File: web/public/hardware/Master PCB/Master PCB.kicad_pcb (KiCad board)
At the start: 2 copper layers, 100 x 100 mm, 98 parts, among them J1 Rows 0-15, J10 LDR2, J11 LDR3, J12 LDR4, J13 SWD Conn, J14 LED Conn, J15 OLED1, J16 OLED2, J17 Relay Conn, J2 Cols 0-21, J3 Cols 22-31, J4 5V_IN, J5 LED1, J6 LED2, J7 LED3, J8 LED4, J9 LDR1, Q1 2N7000, Q2 2N7000, Q3 2N7000, Q4 2N7000, SW1 nRST, SW2 Menu Encoder, U1 STM32U585VITx, U2 M95P32-IXMNT, U3 TLV62568DBV, U4 LM339, U5 MAX7375AXR805, U6 USBLC6-4SC6, U7 USBLC6-2SC6, U8 USBLC6-2SC6

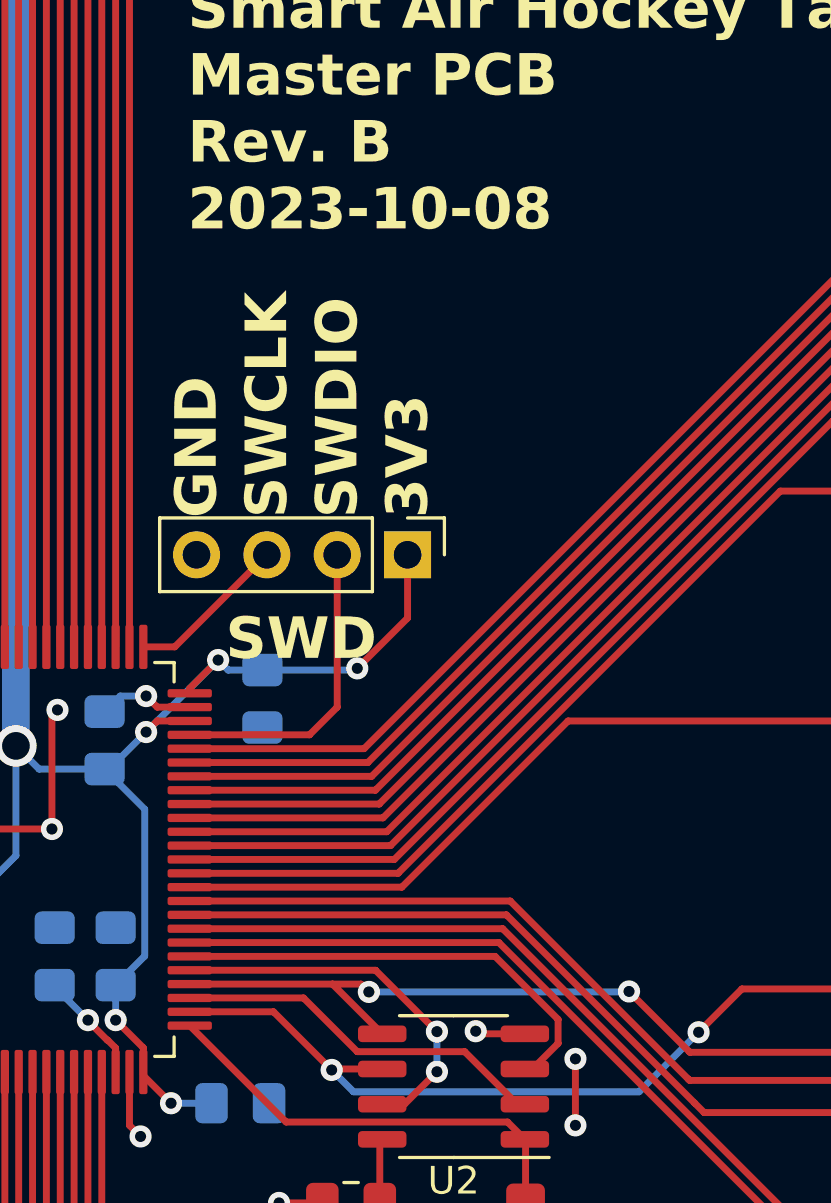
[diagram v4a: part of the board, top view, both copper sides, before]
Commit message: Fix bad trace routing on EEPROM
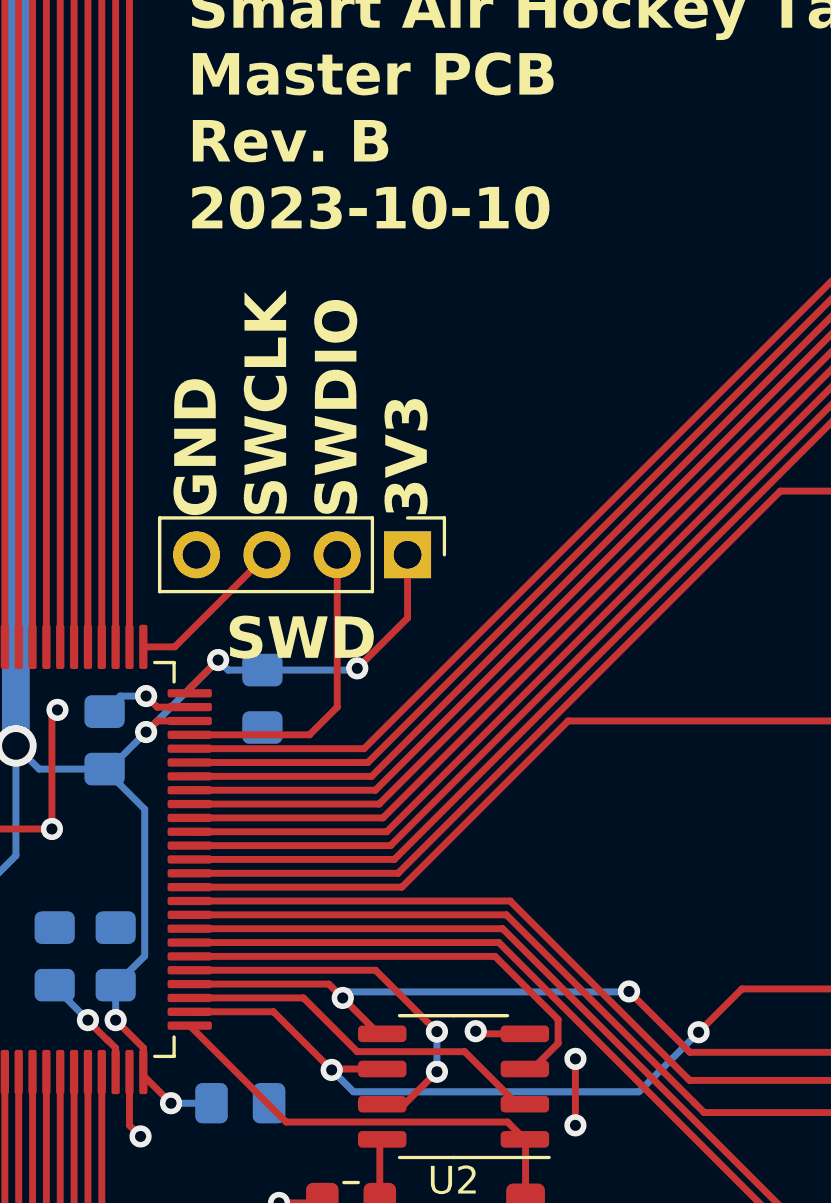
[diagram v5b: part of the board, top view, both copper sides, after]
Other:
- board text added: "ECE 477 Group 5 Smart Air Hockey Table Master PCB Rev. B 2023-10-10"
- board text removed: "ECE 477 Group 5 Smart Air Hockey Table Master PCB Rev. B 2023-10-08"
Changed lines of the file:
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@@
     (effects (font (size 1.5 1.5) (thickness 0.3) bold) (justify top))
   )
-  (gr_text "ECE 477 Group 5\nSmart Air Hockey Table\nMaster PCB\nRev. B\n2023-10-08" (at 157.6 77.4) (layer "F.SilkS")
+  (gr_text "ECE 477 Group 5\nSmart Air Hockey Table\nMaster PCB\nRev. B\n2023-10-10" (at 157.6 77.4) (layer "F.SilkS")
     (effects (font (size 1.5 1.5) (thickness 0.3) bold) (justify left bottom))
   )
@@
   (segment (start 162.8 107.6) (end 163.5895 108.3895) (width 0.25) (layer "B.Cu") (net 42))
   (segment (start 163.5895 108.3895) (end 173.89589 108.3895) (width 0.25) (layer "B.Cu") (net 42))
-  (segment (start 164.625 106.295) (end 162.83 104.5) (width 0.25) (layer "F.Cu") (net 43))
   (segment (start 184.15 106.8625) (end 184.15 105.549503) (width 0.25) (layer "F.Cu") (net 43))
+  (segment (start 164.625 106.295) (end 164.495 106.295) (width 0.25) (layer "F.Cu") (net 43))
   (segment (start 184.15 105.549503) (end 184.100497 105.5) (width 0.25) (layer "F.Cu") (net 43))
+  (segment (start 157.675 104.5) (end 162.7 104.5) (width 0.25) (layer "F.Cu") (net 43))
   (segment (start 198.6755 120.287701) (end 198.6755 112.6755) (width 0.25) (layer "F.Cu") (net 43))
   (segment (start 188.6 108) (end 189.6 109) (width 0.25) (layer "F.Cu") (net 43))
+  (segment (start 164.495 106.295) (end 163.2 105) (width 0.25) (layer "F.Cu") (net 43))
   (segment (start 189.6 109) (end 195 109) (width 0.25) (layer "F.Cu") (net 43))
+  (segment (start 162.7 104.5) (end 163.2 105) (width 0.25) (layer "F.Cu") (net 43))
   (segment (start 184.05 106.9625) (end 184.15 106.8625) (width 0.25) (layer "F.Cu") (net 43))
   (segment (start 195 127) (end 198.712299 123.287701) (width 0.25) (layer "F.Cu") (net 43))
   (segment (start 175.732682 106.9625) (end 184.05 106.9625) (width 0.25) (layer "F.Cu") (net 43))
-  (segment (start 162.83 104.5) (end 163.859902 104.5) (width 0.25) (layer "F.Cu") (net 43))
-  (segment (start 162.83 104.5) (end 157.675 104.5) (width 0.25) (layer "F.Cu") (net 43))
   (segment (start 198.712299 123.287701) (end 198.712299 122.312299) (width 0.25) (layer "F.Cu") (net 43))
   (segment (start 198.6755 112.6755) (end 195 109) (width 0.25) (layer "F.Cu") (net 43))
   (segment (start 173.535091 104.764909) (end 175.732682 106.9625) (width 0.25) (layer "F.Cu") (net 43))
-  (segment (start 163.859902 104.5) (end 164.142201 104.782299) (width 0.25) (layer "F.Cu") (net 43))
   (via (at 198.6755 120.287701) (size 0.8) (drill 0.4) (layers "F.Cu" "B.Cu") (net 43))
-  (via (at 164.142201 104.782299) (size 0.8) (drill 0.4) (layers "F.Cu" "B.Cu") (net 43))
   (via (at 198.712299 122.312299) (size 0.8) (drill 0.4) (layers "F.Cu" "B.Cu") (net 43))
   (via (at 184.100497 105.5) (size 0.8) (drill 0.4) (layers "F.Cu" "B.Cu") (net 43))
   (via (at 173.535091 104.764909) (size 0.8) (drill 0.4) (layers "F.Cu" "B.Cu") (net 43))
   (via (at 188.6 108) (size 0.8) (drill 0.4) (layers "F.Cu" "B.Cu") (net 43))
+  (via (at 163.2 105) (size 0.8) (drill 0.4) (layers "F.Cu" "B.Cu") (net 43))
   (segment (start 198.712299 120.3245) (end 198.6755 120.287701) (width 0.25) (layer "B.Cu") (net 43))
   (segment (start 184.100497 105.525802) (end 186.574695 108) (width 0.25) (layer "B.Cu") (net 43))
   (segment (start 186.574695 108) (end 188.6 108) (width 0.25) (layer "B.Cu") (net 43))
-  (segment (start 164.142201 104.782299) (end 173.517701 104.782299) (width 0.25) (layer "B.Cu") (net 43))
   (segment (start 198.712299 122.312299) (end 198.712299 120.3245) (width 0.25) (layer "B.Cu") (net 43))
-  (segment (start 173.517701 104.782299) (end 173.535091 104.764909) (width 0.25) (layer "B.Cu") (net 43))
+  (segment (start 173.517701 104.782299) (end 163.417701 104.782299) (width 0.25) (layer "B.Cu") (net 43))
+  (segment (start 163.417701 104.782299) (end 163.2 105) (width 0.25) (layer "B.Cu") (net 43))
+  (segment (start 173.535091 104.764909) (end 173.517701 104.782299) (width 0.25) (layer "B.Cu") (net 43))
   (segment (start 184.100497 105.5) (end 184.100497 105.525802) (width 0.25) (layer "B.Cu") (net 43))
   (segment (start 197.912299 126.087701) (end 195 129) (width 0.25) (layer "F.Cu") (net 44))
